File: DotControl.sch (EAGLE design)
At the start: 21 parts, among them CN1 1X4-BIG, J3 USB-MICROB, SW2 Previous, SW5 Previous, SW6 Next, SW8 Ok, U1 ATMEGA328P-MU-QFN32

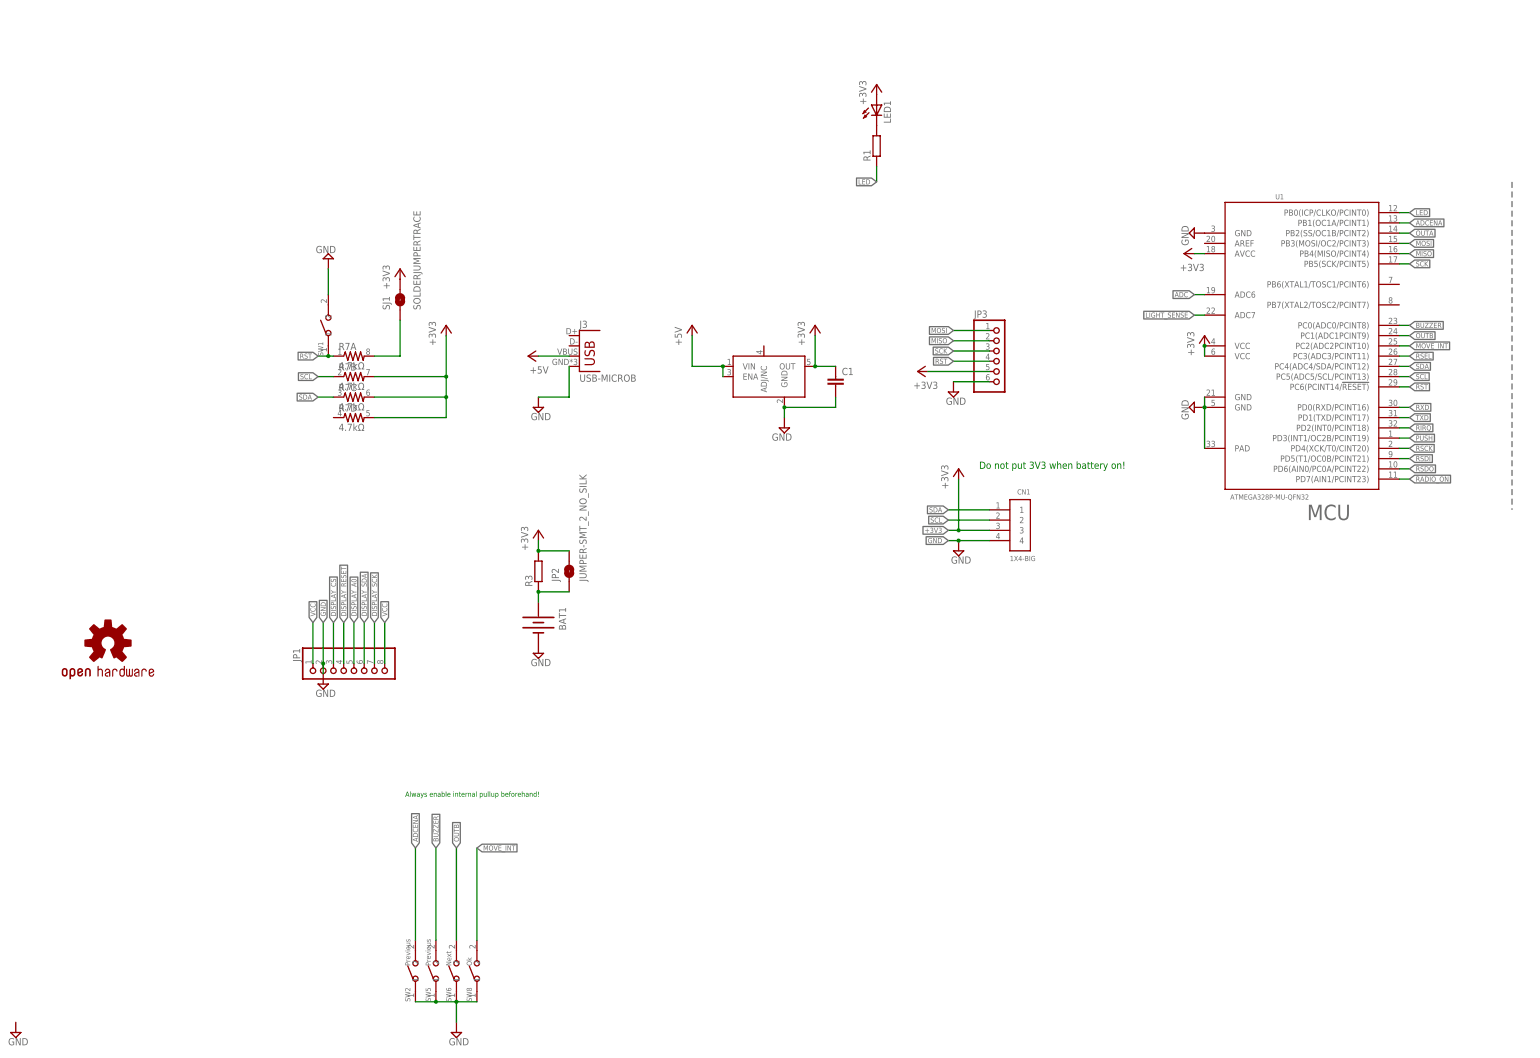
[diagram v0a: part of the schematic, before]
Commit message: Add RGB and crystal
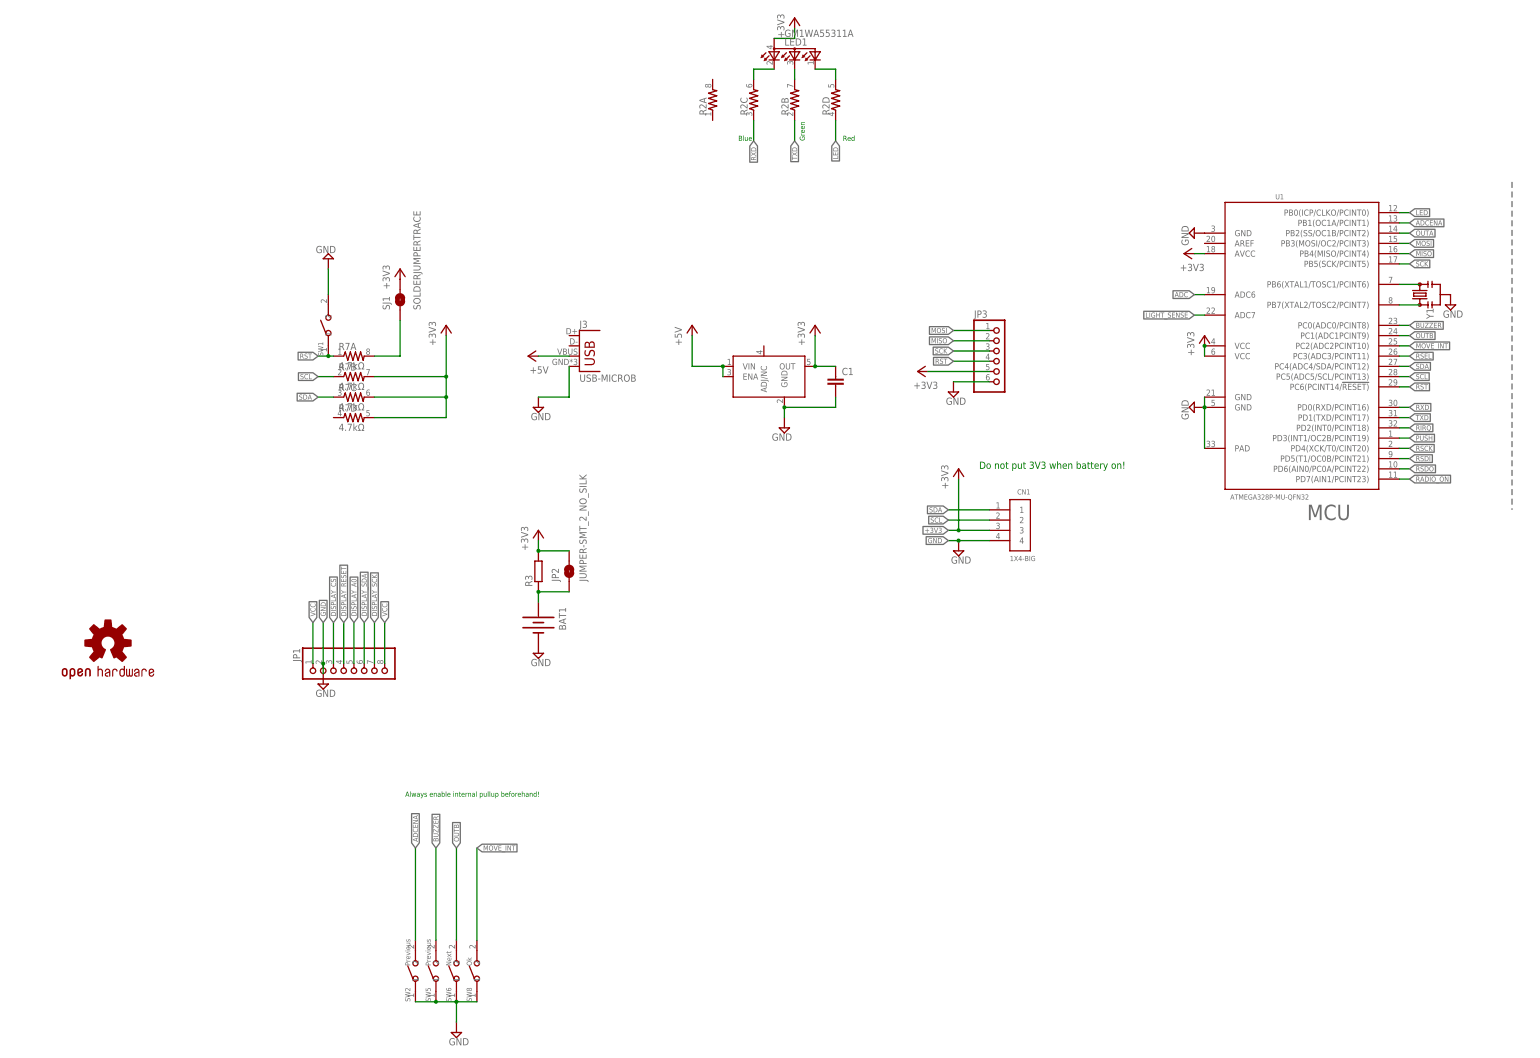
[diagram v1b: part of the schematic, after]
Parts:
- removed R1: (no value), resistor:R-EU_R0603
- added R2: (no value), SparkFun:RESISTOR-ARRAY0603-ARV
- added Y1: (no value), SparkFun-Clocks:RESONATORSMD-3.2X1.3
- LED1: value (none) -> GM1WA55311A; device SparkFun:LED0603 -> led:GM1WA55311A
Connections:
- removed net N$1: LED1.C, R1.2
- new net N$10: LED1.CRED, R2C.2
- new net N$15: LED1.CGREEN, R2D.2
- new net N$6: U1.PB6(XTAL1/TOSC1/PCINT6), Y1.3
- new net N$8: U1.PB7(XTAL2/TOSC2/PCINT7), Y1.1
- new net N$9: LED1.CBLUE, R2B.2
- net GND: now also Y1.2
- net LED: now also R2D.1; no longer R1.1
- net RXD: now also R2C.1
- net TXD: now also R2B.1
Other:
- note added: "Blue"
- note added: "Green"
- note added: "Red"
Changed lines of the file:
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@@
 <part name="SUPPLY13" library="supply2" deviceset="GND" device=""/>
 <part name="SW8" library="Seeed-OPL-Switch" deviceset="SMD-BUTTON(2P-6.0X3.0X2.5MM)" device="-DHT-1163S" value="Ok"/>
-<part name="SUPPLY17" library="supply2" deviceset="GND" device=""/>
 <part name="SUPPLY2" library="supply2" deviceset="GND" device=""/>
 <part name="U$2" library="SparkFun" deviceset="OSHW-LOGO" device="L"/>
@@
 <part name="+3V5" library="supply1" deviceset="+3V3" device=""/>
 <part name="+3V2" library="supply1" deviceset="+3V3" device=""/>
+<part name="Y1" library="SparkFun-Clocks" deviceset="RESONATOR" device="SMD-3.2X1.3"/>
+<part name="SUPPLY30" library="supply2" deviceset="GND" device=""/>
 <part name="SW2" library="Seeed-OPL-Switch" deviceset="SMD-BUTTON(2P-6.0X3.0X2.5MM)" device="-DHT-1163S" value="Previous"/>
 <part name="JP1" library="adafruit" deviceset="PINHD-1X8" device="CLEANBIG"/>
@@
 <part name="+3V3" library="supply1" deviceset="+3V3" device=""/>
 <part name="BAT1" library="Battery" deviceset="BATTERY" device="20PTH"/>
+<part name="+3V14" library="supply1" deviceset="+3V3" device=""/>
+<part name="LED1" library="led" deviceset="GM1WA55311A" device=""/>
+<part name="R2" library="SparkFun" deviceset="RESISTOR-ARRAY" device="0603-ARV"/>
 <part name="+3V1" library="supply1" deviceset="+3V3" device=""/>
 <part name="SUPPLY18" library="supply2" deviceset="GND" device=""/>
@@
 <part name="SJ1" library="SparkFun" deviceset="SOLDERJUMPER" device="TRACE"/>
 <part name="+3V7" library="supply1" deviceset="+3V3" device=""/>
-<part name="R1" library="resistor" deviceset="R-EU_" device="R0603"/>
-<part name="+3V9" library="supply1" deviceset="+3V3" device=""/>
-<part name="LED1" library="SparkFun" deviceset="LED" device="0603"/>
 </parts>
 <sheets>
@@
 <text x="304.8" y="165.1" size="3.81" layer="95">MCU</text>
 <text x="391.16" y="165.1" size="3.81" layer="95">Radio</text>
+<text x="163.83" y="259.08" size="1.27" layer="91">Blue</text>
+<text x="180.34" y="259.08" size="1.27" layer="91" rot="R90">Green</text>
+<text x="189.738" y="259.08" size="1.27" layer="91">Red</text>
 <text x="223.52" y="177.8" size="1.778" layer="91">Do not put 3V3 when battery on!</text>
 <text x="81.28" y="96.52" size="1.27" layer="91">Always enable internal pullup beforehand!</text>
@@
 <instance part="SUPPLY13" gate="GND" x="93.98" y="38.1"/>
 <instance part="SW8" gate="G$1" x="99.06" y="53.34" rot="R90"/>
-<instance part="SUPPLY17" gate="GND" x="-15.24" y="38.1"/>
 <instance part="SUPPLY2" gate="GND" x="60.96" y="124.46"/>
 <instance part="U$2" gate="G$1" x="7.62" y="134.62"/>
@@
 <instance part="+3V5" gate="G$1" x="393.7" y="238.76"/>
 <instance part="+3V2" gate="G$1" x="274.32" y="231.14" rot="R90"/>
+<instance part="Y1" gate="G$1" x="332.74" y="220.98" rot="R90"/>
+<instance part="SUPPLY30" gate="GND" x="340.36" y="218.44"/>
 <instance part="SW2" gate="G$1" x="83.82" y="53.34" rot="R90"/>
 <instance part="JP1" gate="G$1" x="66.04" y="127" rot="MR270"/>
@@
 <instance part="+3V3" gate="G$1" x="114.3" y="162.56"/>
 <instance part="BAT1" gate="G$1" x="114.3" y="139.7" rot="R270"/>
+<instance part="+3V14" gate="G$1" x="177.8" y="289.56"/>
+<instance part="LED1" gate="G$1" x="177.8" y="281.94"/>
+<instance part="R2" gate="A" x="157.48" y="269.24" rot="R90"/>
+<instance part="R2" gate="B" x="177.8" y="269.24" rot="R90"/>
+<instance part="R2" gate="C" x="167.64" y="269.24" rot="R90"/>
+<instance part="R2" gate="D" x="187.96" y="269.24" rot="R90"/>
 <instance part="+3V1" gate="G$1" x="218.44" y="177.8"/>
 <instance part="SUPPLY18" gate="GND" x="218.44" y="157.48"/>
@@
 <instance part="SJ1" gate="1" x="80.01" y="219.71" rot="R90"/>
 <instance part="+3V7" gate="G$1" x="80.01" y="227.33"/>
-<instance part="R1" gate="G$1" x="198.12" y="257.81" rot="R90"/>
-<instance part="+3V9" gate="G$1" x="198.12" y="273.05"/>
-<instance part="LED1" gate="G$1" x="198.12" y="267.97"/>
 </instances>
 <busses>
@@
 <wire x1="393.7" y1="195.58" x2="391.16" y2="195.58" width="0.1524" layer="91"/>
 <junction x="391.16" y="195.58"/>
+</segment>
+<segment>
+<pinref part="Y1" gate="G$1" pin="2"/>
+<pinref part="SUPPLY30" gate="GND" pin="GND"/>
 </segment>
 <segment>
@@
 </segment>
 <segment>
+<pinref part="LED1" gate="G$1" pin="A"/>
+<pinref part="+3V14" gate="G$1" pin="+3V3"/>
+<wire x1="172.72" y1="284.48" x2="177.8" y2="284.48" width="0.1524" layer="91"/>
+<wire x1="177.8" y1="284.48" x2="177.8" y2="287.02" width="0.1524" layer="91"/>
+</segment>
+<segment>
 <wire x1="226.06" y1="162.56" x2="218.44" y2="162.56" width="0.1524" layer="91"/>
 <pinref part="+3V1" gate="G$1" pin="+3V3"/>
@@
 <pinref part="+3V7" gate="G$1" pin="+3V3"/>
 </segment>
-<segment>
-<pinref part="LED1" gate="G$1" pin="A"/>
-<pinref part="+3V9" gate="G$1" pin="+3V3"/>
-</segment>
 </net>
 <net name="PUSH" class="0">
@@
 </segment>
 <segment>
-<pinref part="R1" gate="G$1" pin="1"/>
-<wire x1="198.12" y1="252.73" x2="198.12" y2="248.92" width="0.1524" layer="91"/>
-<label x="198.12" y="248.92" size="1.27" layer="95" rot="R180" xref="yes"/>
+<wire x1="187.96" y1="264.16" x2="187.96" y2="259.08" width="0.1524" layer="91"/>
+<label x="187.96" y="259.08" size="1.27" layer="95" rot="R270" xref="yes"/>
+<pinref part="R2" gate="D" pin="1"/>
 </segment>
 </net>
@@
 <label x="330.2" y="190.5" size="1.27" layer="95" xref="yes"/>
 </segment>
+<segment>
+<wire x1="177.8" y1="264.16" x2="177.8" y2="259.08" width="0.1524" layer="91"/>
+<label x="177.8" y="259.08" size="1.27" layer="95" rot="R270" xref="yes"/>
+<pinref part="R2" gate="B" pin="1"/>
+</segment>
 </net>
 <net name="MOVE_INT" class="0">
@@
 <label x="330.2" y="193.04" size="1.27" layer="95" xref="yes"/>
 </segment>
+<segment>
+<wire x1="167.64" y1="264.16" x2="167.64" y2="259.08" width="0.1524" layer="91"/>
+<label x="167.64" y="259.08" size="1.27" layer="95" rot="R270" xref="yes"/>
+<pinref part="R2" gate="C" pin="1"/>
+</segment>
 </net>
 <net name="OUTB" class="0">
@@
 </segment>
 </net>
+<net name="N$6" class="0">
+<segment>
+<pinref part="U1" gate="G$1" pin="PB6(XTAL1/TOSC1/PCINT6)"/>
+<pinref part="Y1" gate="G$1" pin="3"/>
+<wire x1="332.74" y1="223.52" x2="327.66" y2="223.52" width="0.1524" layer="91"/>
+</segment>
+</net>
+<net name="N$8" class="0">
+<segment>
+<pinref part="U1" gate="G$1" pin="PB7(XTAL2/TOSC2/PCINT7)"/>
+<pinref part="Y1" gate="G$1" pin="1"/>
+<wire x1="332.74" y1="218.44" x2="327.66" y2="218.44" width="0.1524" layer="91"/>
+</segment>
+</net>
 <net name="RADIO_ON" class="0">
 <segment>
@@
 <wire x1="327.66" y1="175.26" x2="330.2" y2="175.26" width="0.1524" layer="91"/>
 <label x="330.2" y="175.26" size="1.27" layer="95" xref="yes"/>
+</segment>
+</net>
+<net name="N$9" class="0">
+<segment>
+<pinref part="LED1" gate="G$1" pin="CBLUE"/>
+<wire x1="177.8" y1="276.86" x2="177.8" y2="274.32" width="0.1524" layer="91"/>
+<pinref part="R2" gate="B" pin="2"/>
+</segment>
+</net>
+<net name="N$15" class="0">
+<segment>
+<pinref part="LED1" gate="G$1" pin="CGREEN"/>
+<wire x1="187.96" y1="274.32" x2="187.96" y2="276.86" width="0.1524" layer="91"/>
+<wire x1="187.96" y1="276.86" x2="182.88" y2="276.86" width="0.1524" layer="91"/>
+<pinref part="R2" gate="D" pin="2"/>
+</segment>
+</net>
+<net name="N$10" class="0">
+<segment>
+<pinref part="LED1" gate="G$1" pin="CRED"/>
+<wire x1="172.72" y1="276.86" x2="167.64" y2="276.86" width="0.1524" layer="91"/>
+<wire x1="167.64" y1="276.86" x2="167.64" y2="274.32" width="0.1524" layer="91"/>
+<pinref part="R2" gate="C" pin="2"/>
 </segment>
 </net>
@@
 </segment>
 </net>
-<net name="N$1" class="0">
-<segment>
-<pinref part="R1" gate="G$1" pin="2"/>
-<pinref part="LED1" gate="G$1" pin="C"/>
-</segment>
-</net>

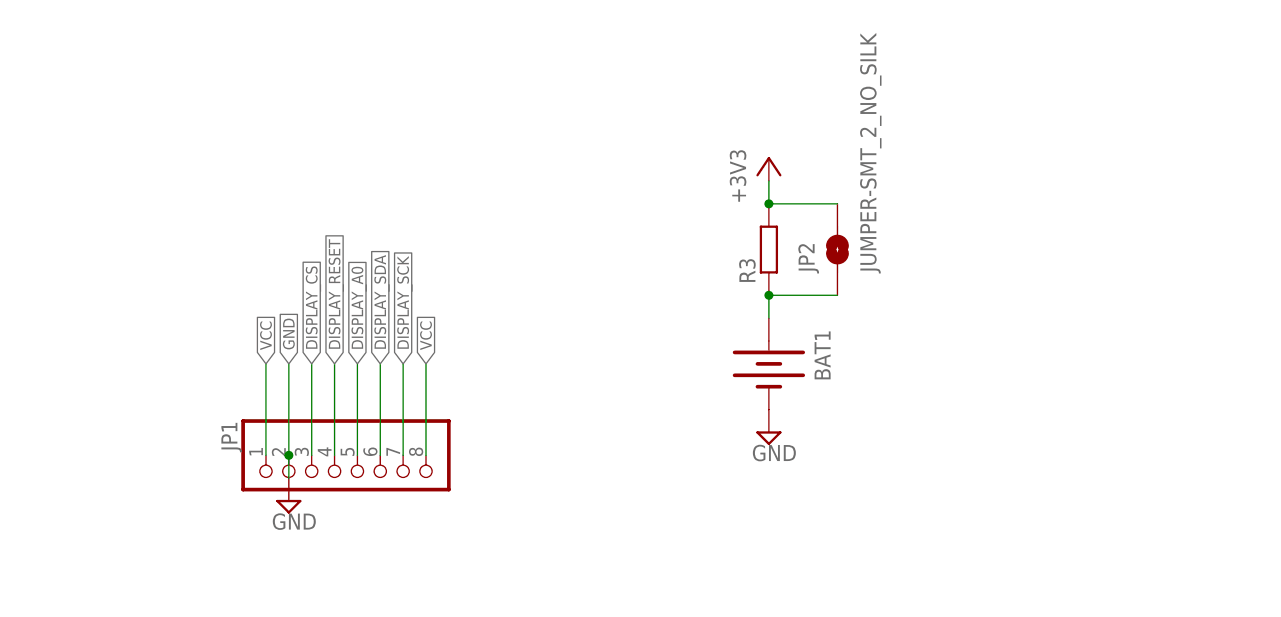
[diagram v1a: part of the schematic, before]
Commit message: Add charging led
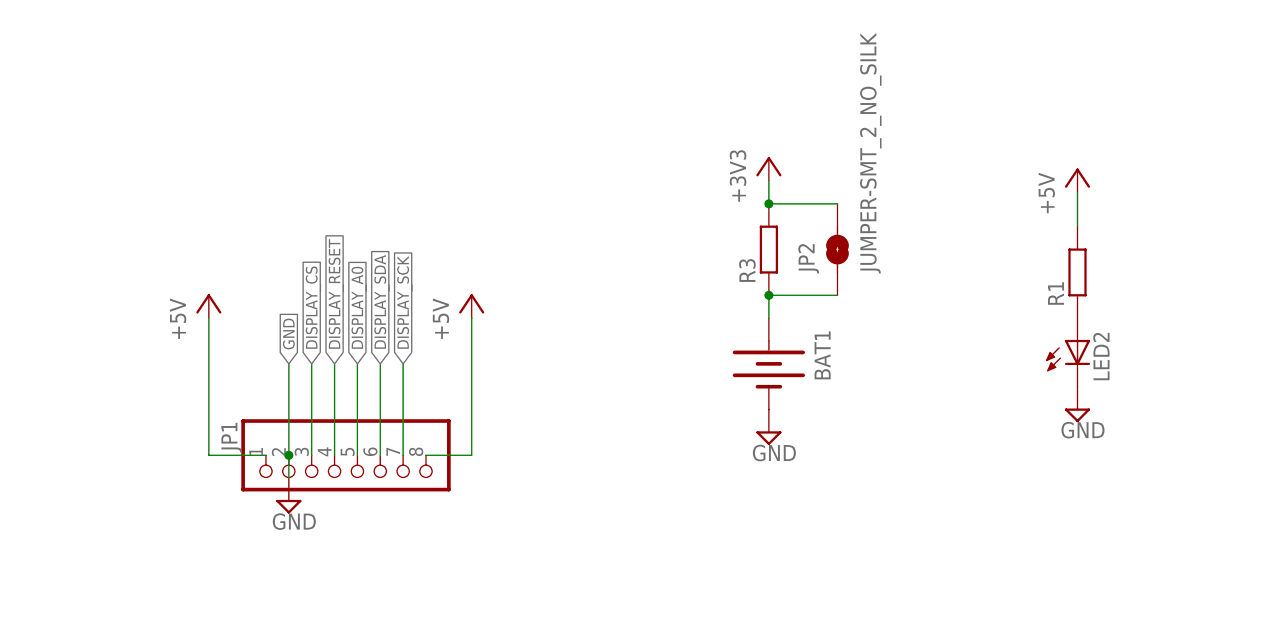
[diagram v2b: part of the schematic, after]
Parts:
- added LED2: (no value), SparkFun:LED0603
- added R1: (no value), resistor:R-EU_R0603
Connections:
- removed net VCC: JP1.1, JP1.8
- new net N$1: LED2.A, R1.1
- net +5V: now also JP1.1, JP1.8, R1.2
- net GND: now also LED2.C
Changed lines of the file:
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@@
 <part name="SJ1" library="SparkFun" deviceset="SOLDERJUMPER" device="TRACE"/>
 <part name="+3V7" library="supply1" deviceset="+3V3" device=""/>
+<part name="R1" library="resistor" deviceset="R-EU_" device="R0603"/>
+<part name="LED2" library="SparkFun" deviceset="LED" device="0603"/>
+<part name="SUPPLY5" library="supply2" deviceset="GND" device=""/>
+<part name="P+1" library="supply1" deviceset="+5V" device=""/>
+<part name="P+2" library="supply1" deviceset="+5V" device=""/>
+<part name="P+5" library="supply1" deviceset="+5V" device=""/>
 </parts>
 <sheets>
@@
 <instance part="SJ1" gate="1" x="80.01" y="219.71" rot="R90"/>
 <instance part="+3V7" gate="G$1" x="80.01" y="227.33"/>
+<instance part="R1" gate="G$1" x="148.59" y="149.86" rot="R90"/>
+<instance part="LED2" gate="G$1" x="148.59" y="142.24"/>
+<instance part="SUPPLY5" gate="GND" x="148.59" y="134.62"/>
+<instance part="P+1" gate="1" x="81.28" y="147.32"/>
+<instance part="P+2" gate="1" x="52.07" y="147.32"/>
+<instance part="P+5" gate="1" x="148.59" y="161.29"/>
 </instances>
 <busses>
 </busses>
 <nets>
-<net name="VCC" class="0">
-<segment>
-<wire x1="58.42" y1="129.54" x2="58.42" y2="139.7" width="0.1524" layer="91"/>
-<label x="58.42" y="139.7" size="1.27" layer="95" rot="R90" xref="yes"/>
-<pinref part="JP1" gate="G$1" pin="1"/>
-</segment>
-<segment>
-<wire x1="76.2" y1="129.54" x2="76.2" y2="139.7" width="0.1524" layer="91"/>
-<label x="76.2" y="139.7" size="1.27" layer="95" rot="R90" xref="yes"/>
-<pinref part="JP1" gate="G$1" pin="8"/>
-</segment>
-</net>
 <net name="GND" class="0">
 <segment>
@@
 <pinref part="SUPPLY19" gate="GND" pin="GND"/>
 <wire x1="62.23" y1="220.98" x2="62.23" y2="227.33" width="0.1524" layer="91"/>
+</segment>
+<segment>
+<pinref part="LED2" gate="G$1" pin="C"/>
+<pinref part="SUPPLY5" gate="GND" pin="GND"/>
 </segment>
 </net>
@@
 <junction x="160.02" y="203.2"/>
 </segment>
+<segment>
+<pinref part="P+1" gate="1" pin="+5V"/>
+<wire x1="81.28" y1="144.78" x2="81.28" y2="129.54" width="0.1524" layer="91"/>
+<pinref part="JP1" gate="G$1" pin="8"/>
+<wire x1="76.2" y1="129.54" x2="81.28" y2="129.54" width="0.1524" layer="91"/>
+</segment>
+<segment>
+<pinref part="P+2" gate="1" pin="+5V"/>
+<pinref part="JP1" gate="G$1" pin="1"/>
+<wire x1="52.07" y1="144.78" x2="52.07" y2="129.54" width="0.1524" layer="91"/>
+<wire x1="52.07" y1="129.54" x2="58.42" y2="129.54" width="0.1524" layer="91"/>
+</segment>
+<segment>
+<pinref part="R1" gate="G$1" pin="2"/>
+<wire x1="148.59" y1="154.94" x2="148.59" y2="158.75" width="0.1524" layer="91"/>
+<pinref part="P+5" gate="1" pin="+5V"/>
+</segment>
 </net>
 <net name="MOSI" class="0">
@@
 </segment>
 </net>
+<net name="N$1" class="0">
+<segment>
+<pinref part="R1" gate="G$1" pin="1"/>
+<pinref part="LED2" gate="G$1" pin="A"/>
+</segment>
+</net>
